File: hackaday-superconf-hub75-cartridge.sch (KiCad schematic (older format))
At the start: 6 parts, among them J1 Conn_02x06_Odd_Even, J2 Conn_02x20_Odd_Even, J3 Conn_02x08_Odd_Even, J4 Conn_01x01, U1 M25PX32-VMW

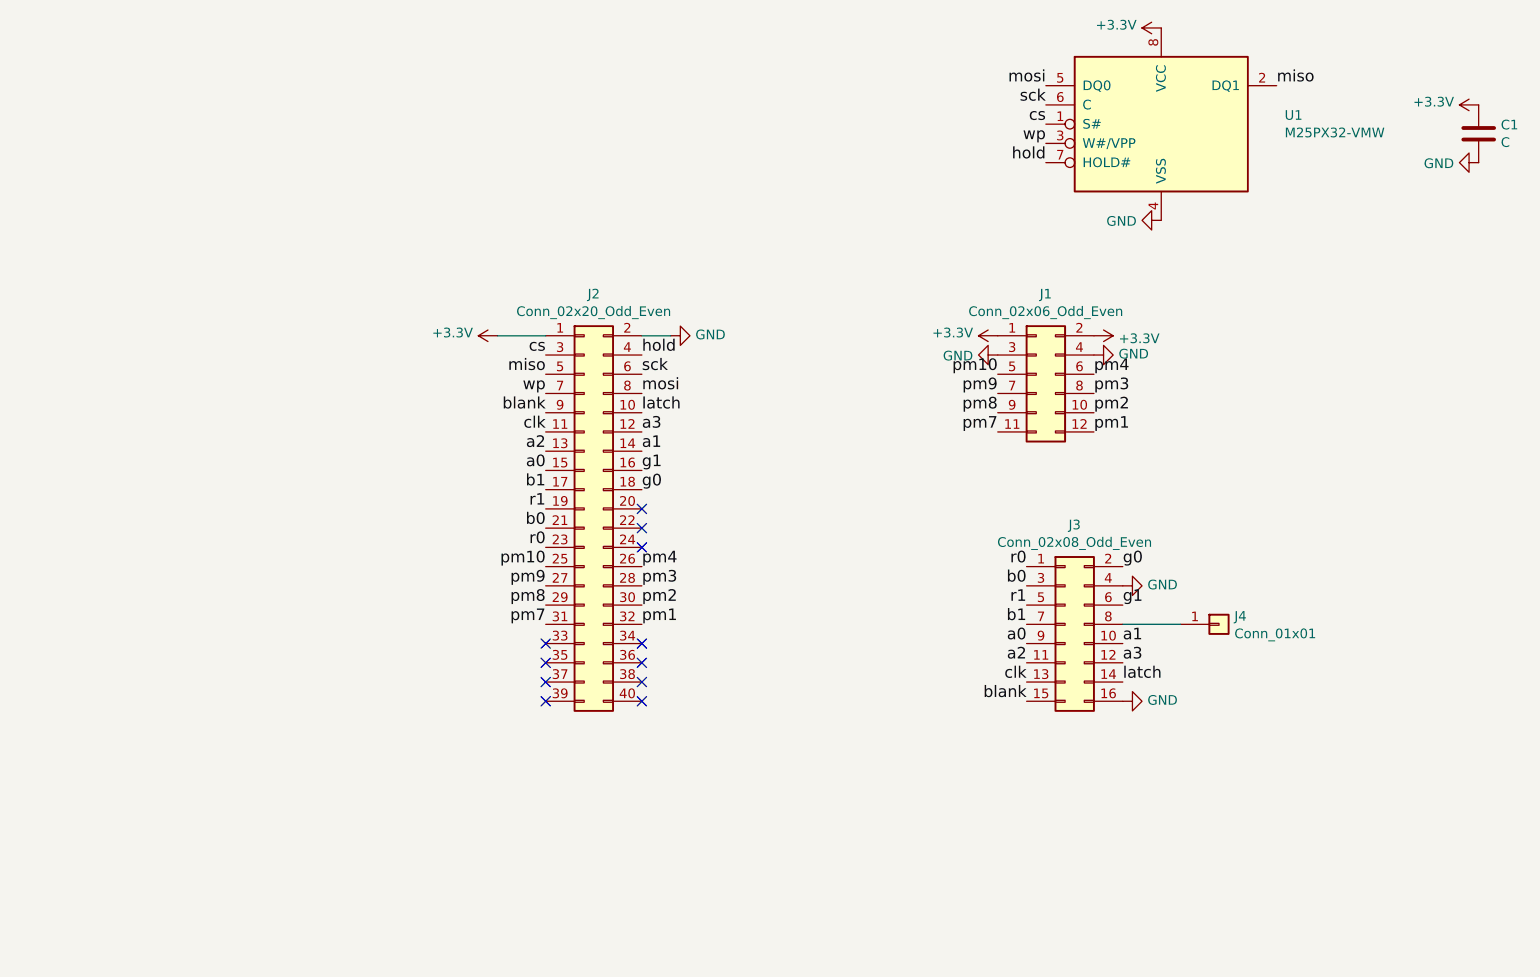
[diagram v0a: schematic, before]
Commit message: added farnell part nums
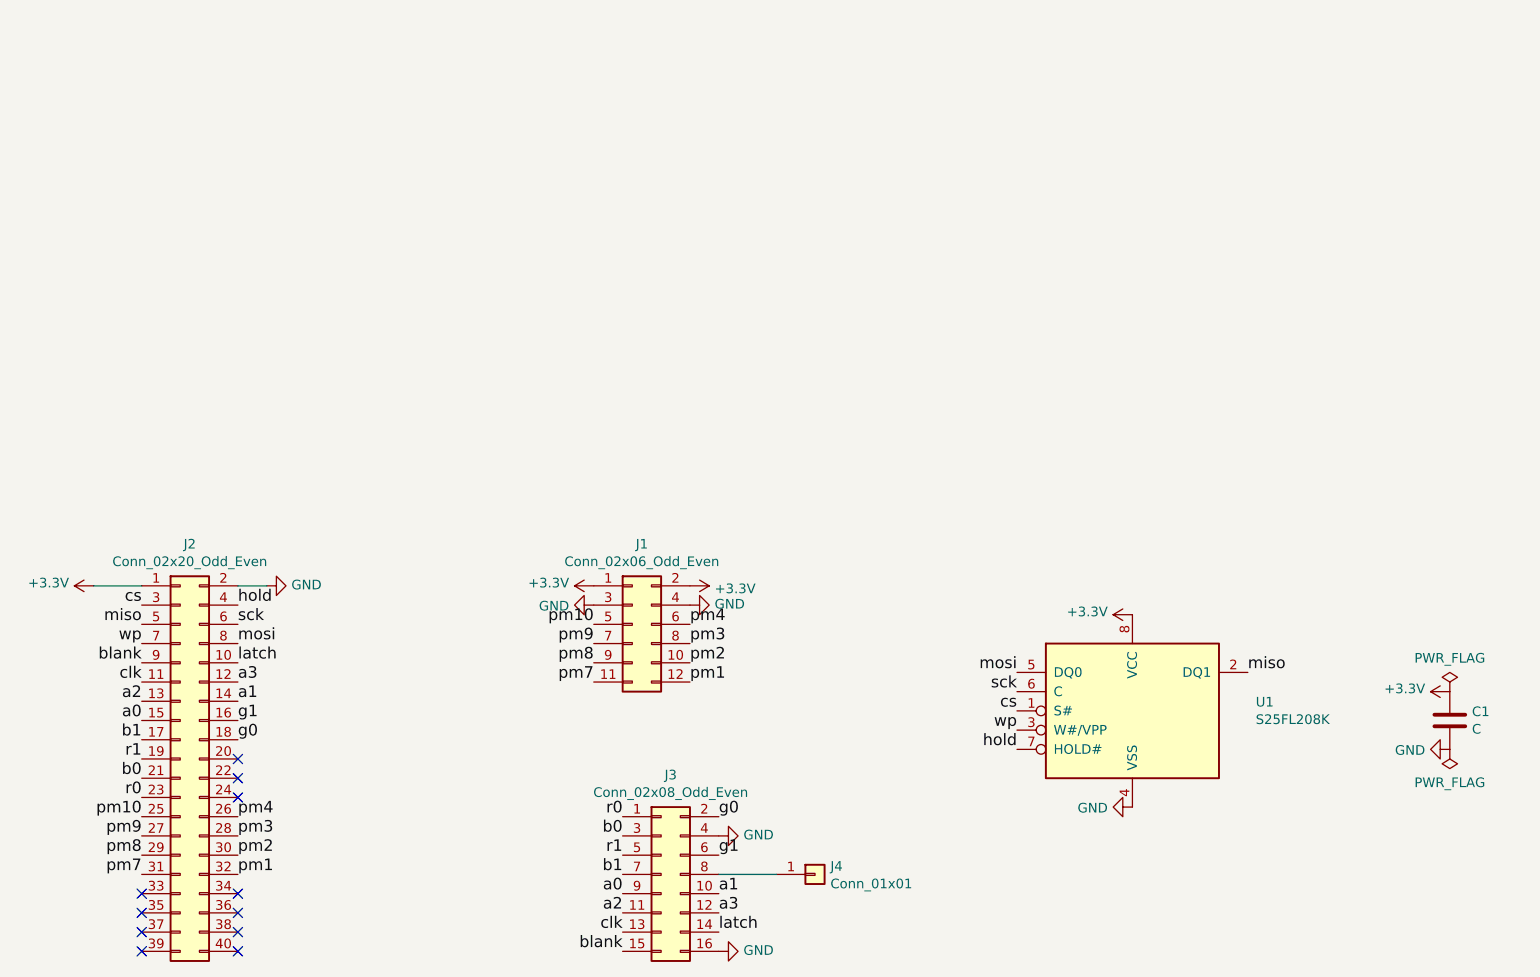
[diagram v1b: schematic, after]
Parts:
- J1: MOQ (none) -> Value; farnell # (none) -> 1593452; leadtime (none) -> Value; supplier (none) -> Value; supplier PN (none) -> Value
- J2: MOQ (none) -> Value; farnell # (none) -> 2847214; leadtime (none) -> Value; supplier (none) -> Value; supplier PN (none) -> Value
- J3: MOQ (none) -> Value; farnell # (none) -> 2843530; leadtime (none) -> Value; supplier (none) -> Value; supplier PN (none) -> Value
- U1: value M25PX32-VMW -> S25FL208K; MOQ (none) -> Value; farnell # (none) -> 2340553; leadtime (none) -> Value; supplier (none) -> Value; supplier PN (none) -> Value
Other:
- moved on the sheet: C1, J1, J2, J3, J4, U1
